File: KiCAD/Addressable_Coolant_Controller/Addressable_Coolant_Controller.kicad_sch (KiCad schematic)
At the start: 2 parts, among them J1 XW4M-10D2-H1DS, J2 XW4M-02D1-H1DA

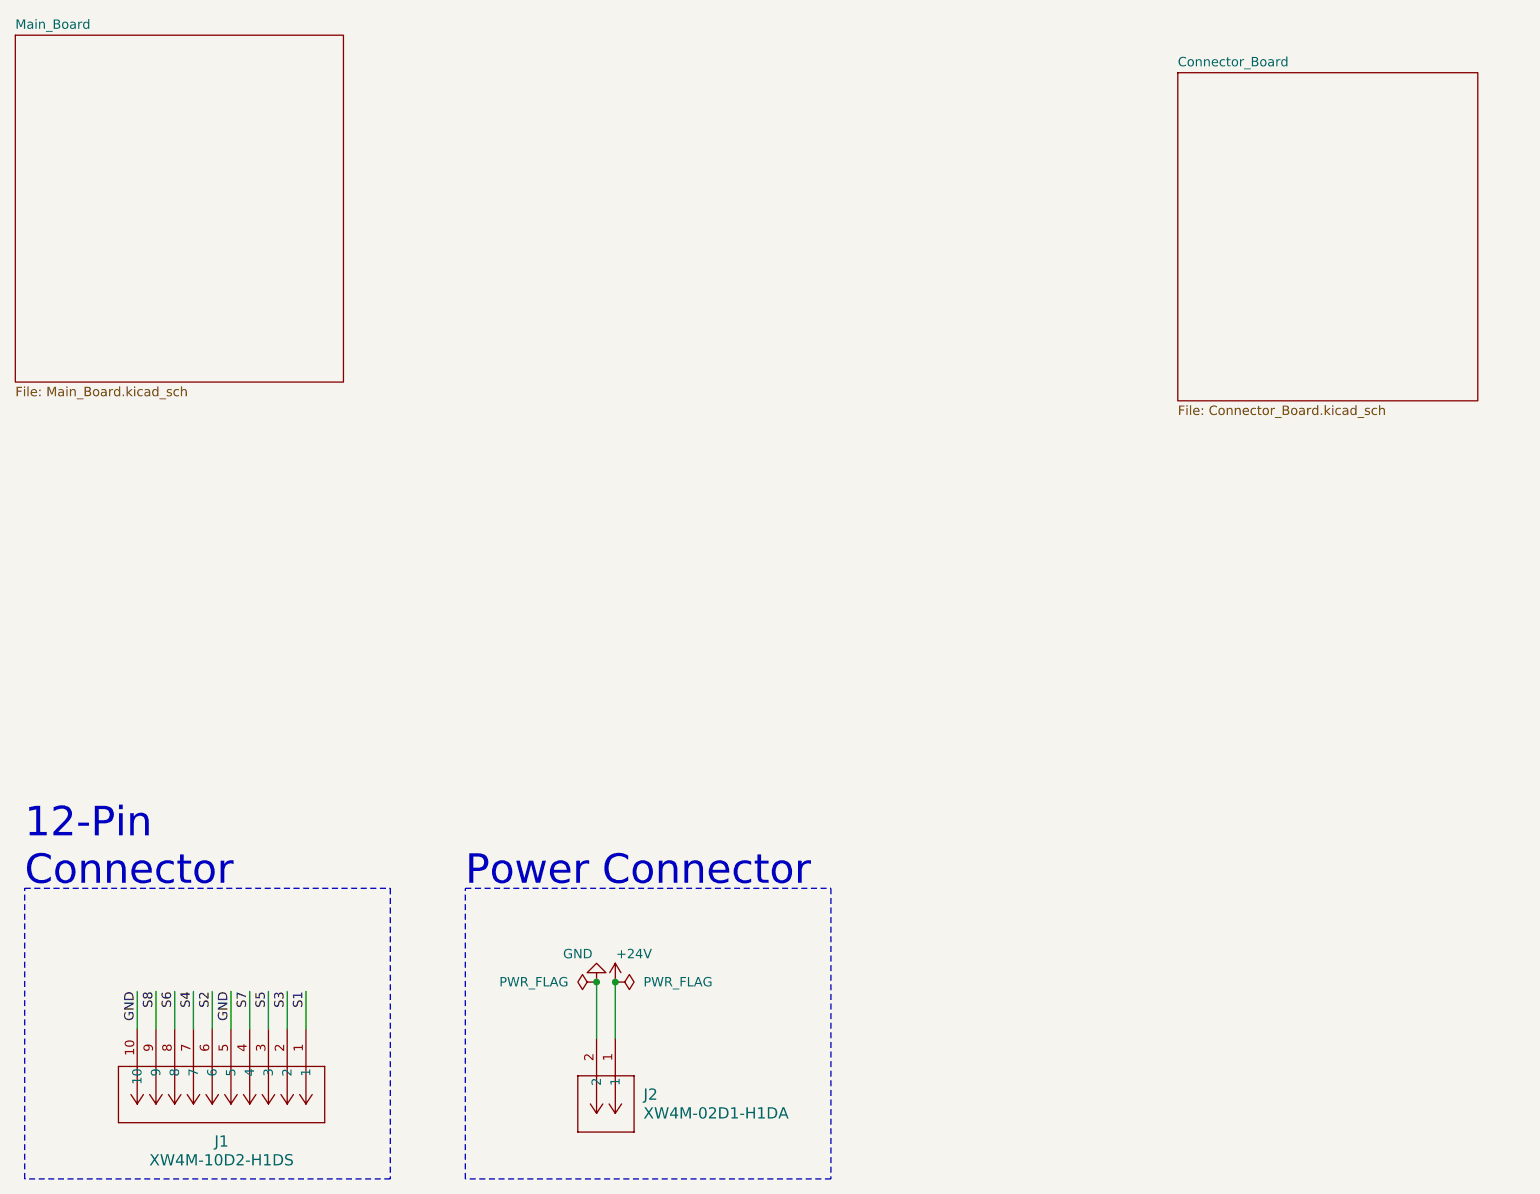
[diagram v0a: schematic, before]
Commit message: Updating KiCAD project to multi-board structure
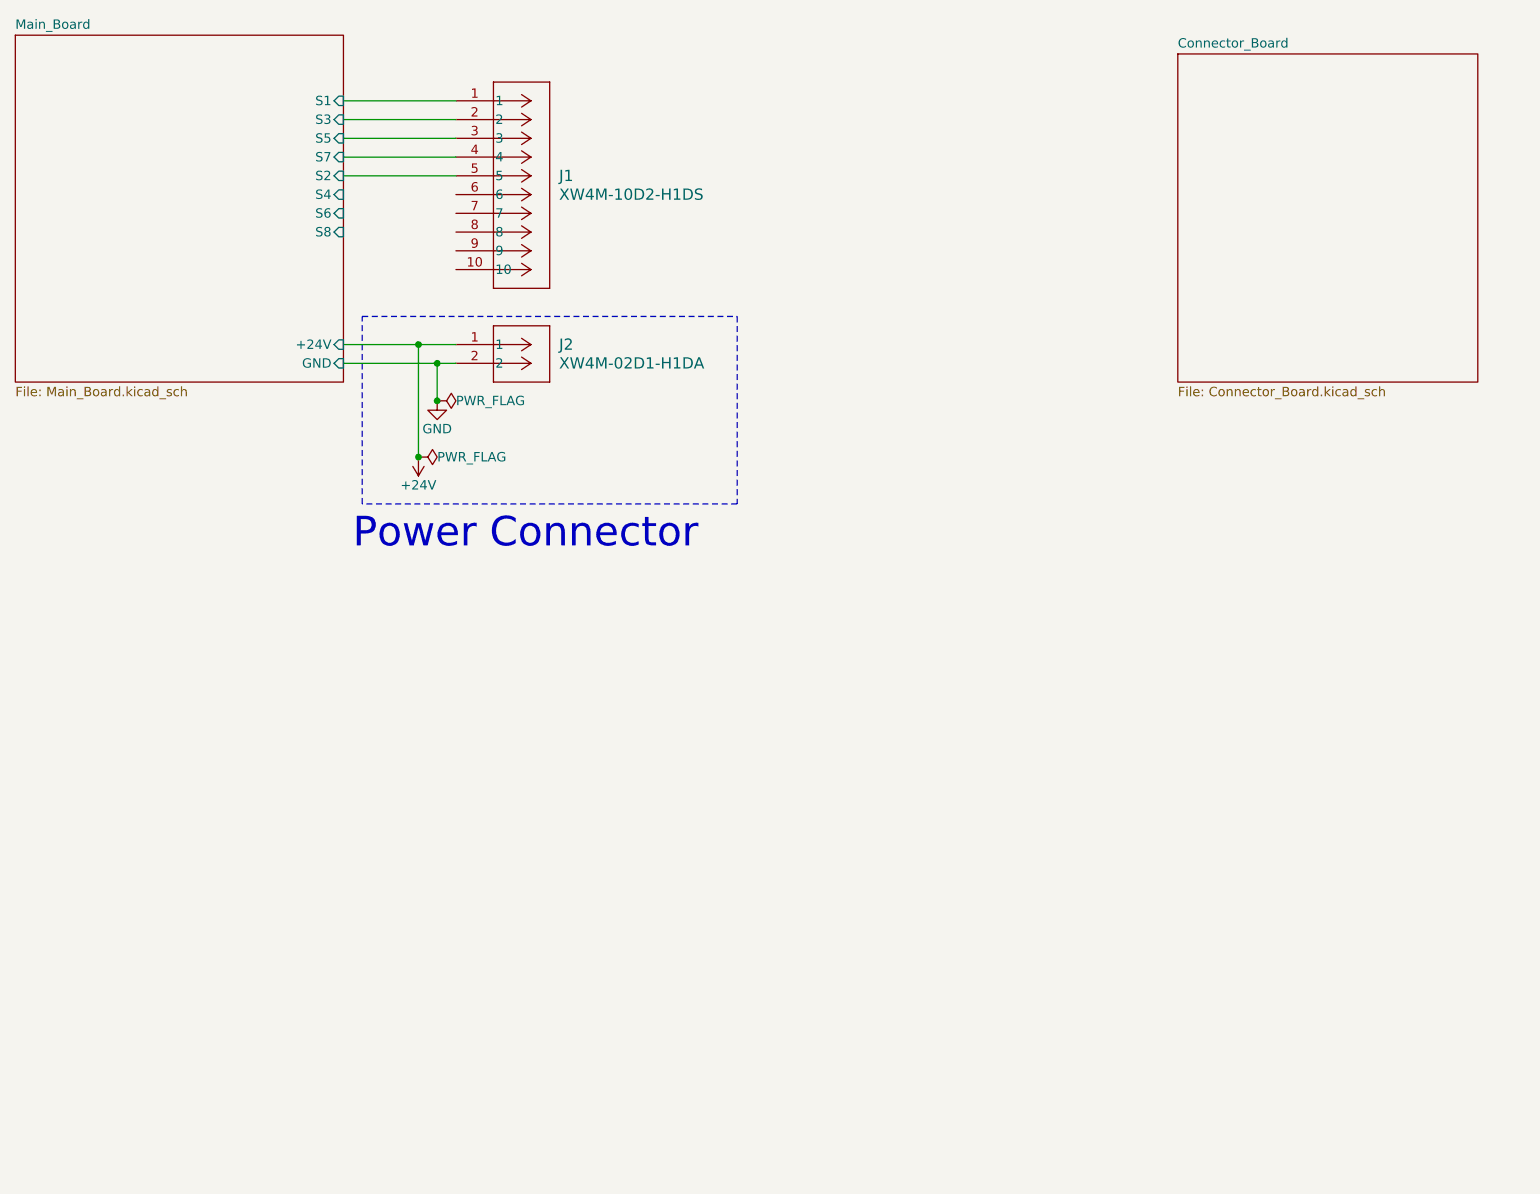
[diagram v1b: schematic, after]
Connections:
- net GND: no longer J1.10, J1.5
- net S1 renamed Main_Board/S1
- net S2: no longer names the net of J1.6
- net S3 renamed Main_Board/S3
- net S4: no longer names the net of J1.7
- net S5 renamed Main_Board/S5
- net S6: no longer names the net of J1.8
- net S7 renamed Main_Board/S7
- net S8: no longer names the net of J1.9
- new net Main_Board/S2: J1.5
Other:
- sheet Main_Board ports: added +24V, GND, S1, S2, S3, S4, S5, S6, S7, S8; removed none
- note removed: "12-Pin Connector"

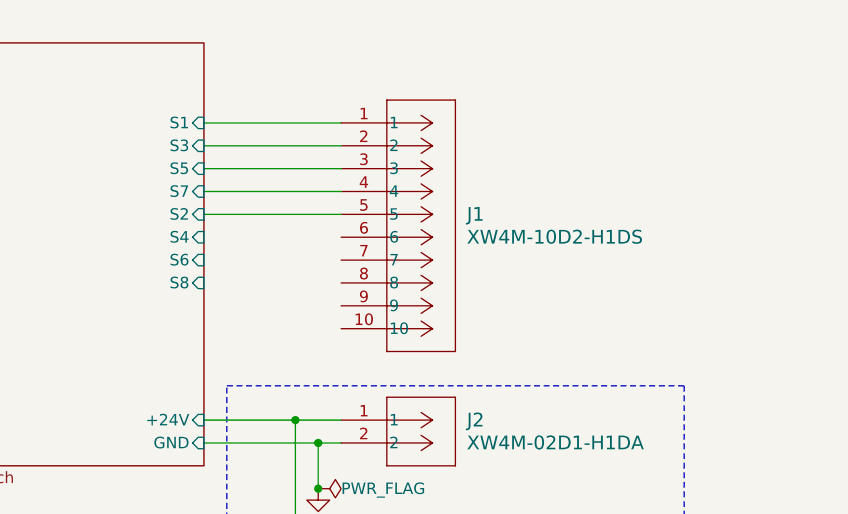
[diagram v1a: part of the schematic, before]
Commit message: Updating wiring positions to match 12 pin connector
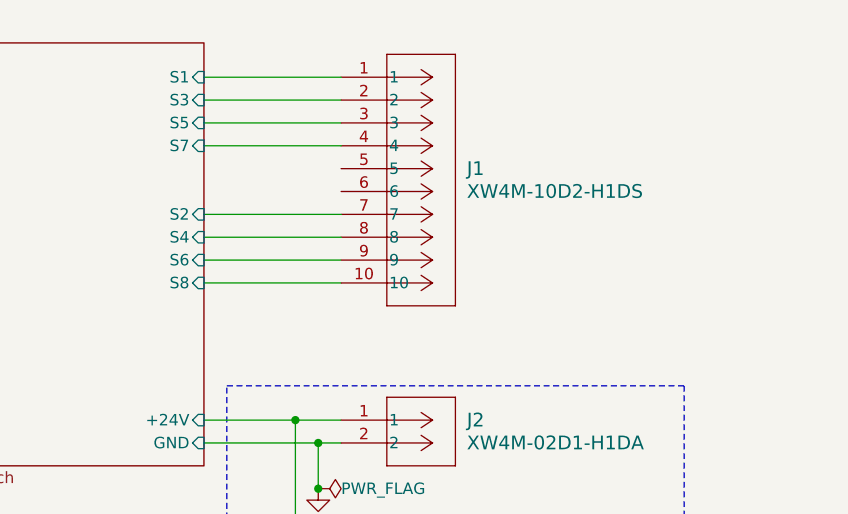
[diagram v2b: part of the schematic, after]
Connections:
- net Main_Board/S2: now also J1.7; no longer J1.5
- net Main_Board/S4: now also J1.8
- net Main_Board/S6: now also J1.9
- net Main_Board/S8: now also J1.10
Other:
- moved on the sheet: J1
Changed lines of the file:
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@@
   (junction (at 82.55 71.12) (diameter 0) (color 0 0 0 0)
   )
-  (wire (pts (xy 72.39 45.72) (xy 87.63 45.72))
+  (wire (pts (xy 72.39 55.88) (xy 87.63 55.88))
+    (stroke (width 0) (type default))
+  )
+  (wire (pts (xy 72.39 40.64) (xy 87.63 40.64))
+    (stroke (width 0) (type default))
+  )
+  (wire (pts (xy 72.39 50.8) (xy 87.63 50.8))
     (stroke (width 0) (type default))
   )
@@
     (stroke (width 0) (type default))
   )
+  (wire (pts (xy 72.39 33.02) (xy 87.63 33.02))
+    (stroke (width 0) (type default))
+  )
   (wire (pts (xy 72.39 38.1) (xy 87.63 38.1))
     (stroke (width 0) (type default))
   )
-  (wire (pts (xy 72.39 43.18) (xy 87.63 43.18))
+  (wire (pts (xy 72.39 71.12) (xy 82.55 71.12))
+    (stroke (width 0) (type default))
+  )
+  (wire (pts (xy 85.09 73.66) (xy 87.63 73.66))
     (stroke (width 0) (type default))
   )
@@
     (stroke (width 0) (type default))
   )
-  (wire (pts (xy 72.39 71.12) (xy 82.55 71.12))
-    (stroke (width 0) (type default))
-  )
-  (wire (pts (xy 85.09 73.66) (xy 87.63 73.66))
-    (stroke (width 0) (type default))
-  )
   (wire (pts (xy 72.39 73.66) (xy 85.09 73.66))
     (stroke (width 0) (type default))
@@
     (stroke (width 0) (type default))
   )
-  (wire (pts (xy 72.39 40.64) (xy 87.63 40.64))
+  (wire (pts (xy 72.39 53.34) (xy 87.63 53.34))
+    (stroke (width 0) (type default))
+  )
+  (wire (pts (xy 72.39 35.56) (xy 87.63 35.56))
     (stroke (width 0) (type default))
   )
@@
     )
   )
-  (symbol (lib_id "xw4m-10d2-h1ds:XW4M-10D2-H1DS") (at 87.63 38.1 0) (unit 1)
+  (symbol (lib_id "xw4m-10d2-h1ds:XW4M-10D2-H1DS") (at 87.63 33.02 0) (unit 1)
     (in_bom yes) (on_board yes) (dnp no) (fields_autoplaced)
-    (property "Reference" "J1" (at 101.6 48.26 0)
-      (effects (font (size 1.524 1.524)) (justify left))
-    )
-    (property "Value" "XW4M-10D2-H1DS" (at 101.6 50.8 0)
-      (effects (font (size 1.524 1.524)) (justify left))
-    )
-    (property "Footprint" "xw4m-10d2-h1ds:xw4m-10d2-h1ds" (at 87.63 38.1 0)
-      (effects (font (size 1.27 1.27) italic) hide)
-    )
-    (property "Datasheet" "XW4M-10D2-H1DS" (at 87.63 38.1 0)
+    (property "Reference" "J1" (at 101.6 43.18 0)
+      (effects (font (size 1.524 1.524)) (justify left))
+    )
+    (property "Value" "XW4M-10D2-H1DS" (at 101.6 45.72 0)
+      (effects (font (size 1.524 1.524)) (justify left))
+    )
+    (property "Footprint" "xw4m-10d2-h1ds:xw4m-10d2-h1ds" (at 87.63 33.02 0)
+      (effects (font (size 1.27 1.27) italic) hide)
+    )
+    (property "Datasheet" "XW4M-10D2-H1DS" (at 87.63 33.02 0)
       (effects (font (size 1.27 1.27) italic) hide)
     )
@@
       (effects (font (size 1.27 1.27)) (justify right))
     )
-    (pin "S7" input (at 72.39 45.72 0)
+    (pin "S7" input (at 72.39 40.64 0)
       (effects (font (size 1.27 1.27)) (justify right))
     )
@@
       (effects (font (size 1.27 1.27)) (justify right))
     )
-    (pin "S5" input (at 72.39 43.18 0)
+    (pin "S5" input (at 72.39 38.1 0)
       (effects (font (size 1.27 1.27)) (justify right))
     )
@@
       (effects (font (size 1.27 1.27)) (justify right))
     )
-    (pin "S3" input (at 72.39 40.64 0)
-      (effects (font (size 1.27 1.27)) (justify right))
-    )
-    (pin "S1" input (at 72.39 38.1 0)
-      (effects (font (size 1.27 1.27)) (justify right))
-    )
+    (pin "S3" input (at 72.39 35.56 0)
+      (effects (font (size 1.27 1.27)) (justify right))
+    )
+    (pin "S1" input (at 72.39 33.02 0)
+      (effects (font (size 1.27 1.27)) (justify right))
+    )

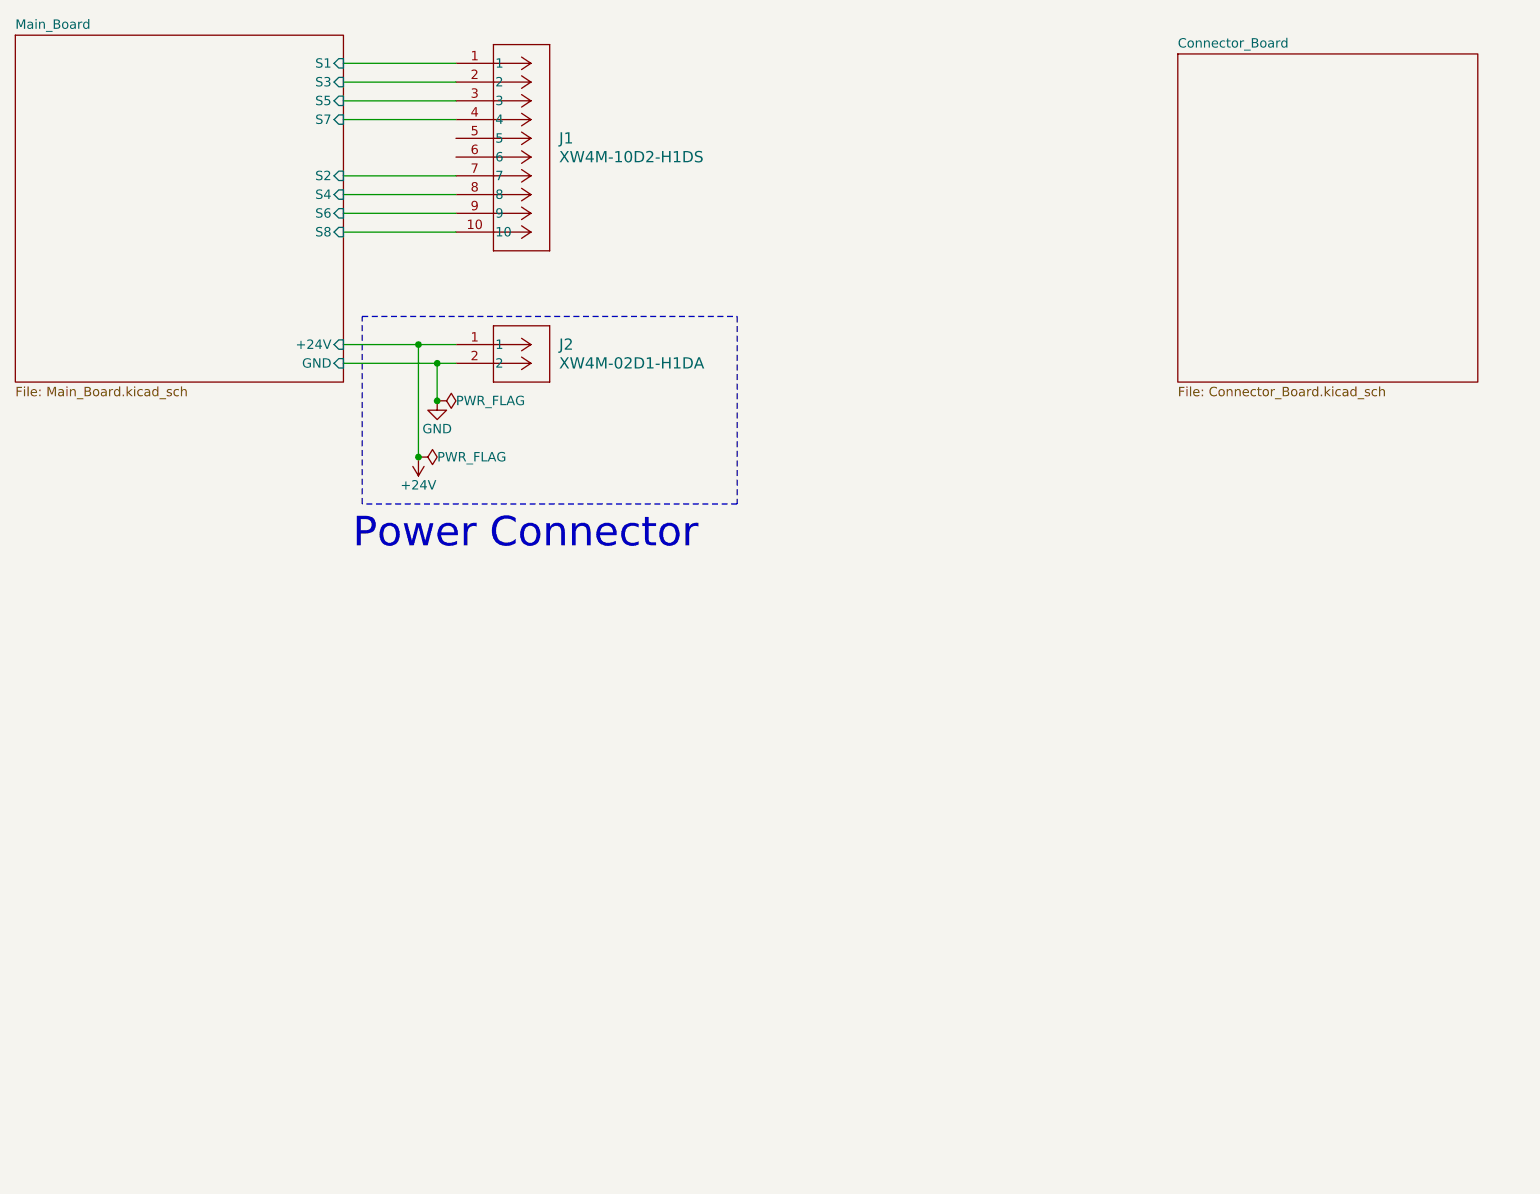
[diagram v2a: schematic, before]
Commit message: Added voltage divider and changed to 12 pin connectors
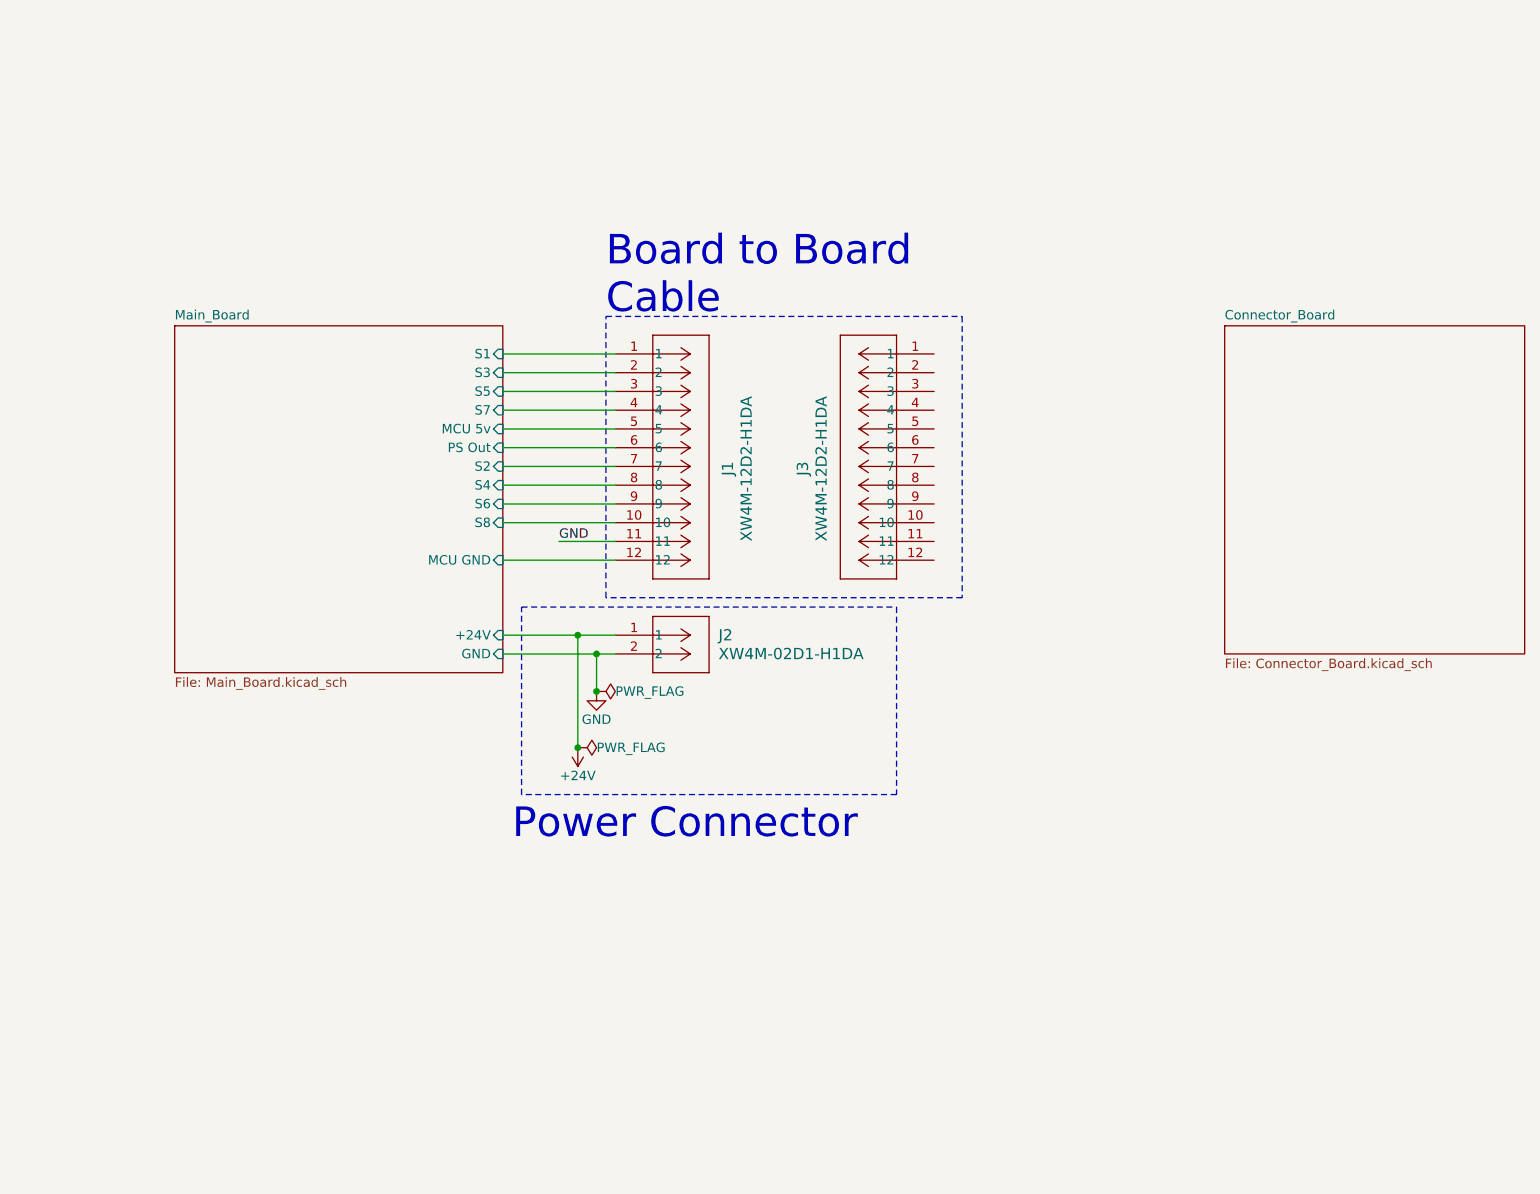
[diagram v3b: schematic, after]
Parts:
- removed J1: XW4M-10D2-H1DS, xw4m-10d2-h1ds:xw4m-10d2-h1ds, symbol xw4m-10d2-h1ds:XW4M-10D2-H1DS
- added J1, J3: XW4M-12D2-H1DA, xw4m-12d2-h1da:xw4m-12d2-h1da, symbol xw4m-12d2-h1da:XW4M-12D2-H1DA
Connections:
- net GND: now also J1.11
- net Main_Board/S1: now also J1.1
- net Main_Board/S2: now also J1.7
- net Main_Board/S3: now also J1.2
- net Main_Board/S4: now also J1.8
- net Main_Board/S5: now also J1.3
- net Main_Board/S6: now also J1.9
- net Main_Board/S7: now also J1.4
- net Main_Board/S8: now also J1.10
- new net Main_Board/MCU 5v: J1.5
- new net Main_Board/MCU GND: J1.12
- new net Main_Board/PS Out: J1.6
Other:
- sheet Main_Board ports: added MCU 5v, MCU GND, PS Out; removed none
- note added: "Board to Board Cable"
- moved on the sheet: J2
